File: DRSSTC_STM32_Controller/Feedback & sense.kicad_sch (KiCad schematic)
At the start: 24 parts, among them J8 Screw_Terminal_01x02, J9 Screw_Terminal_01x02

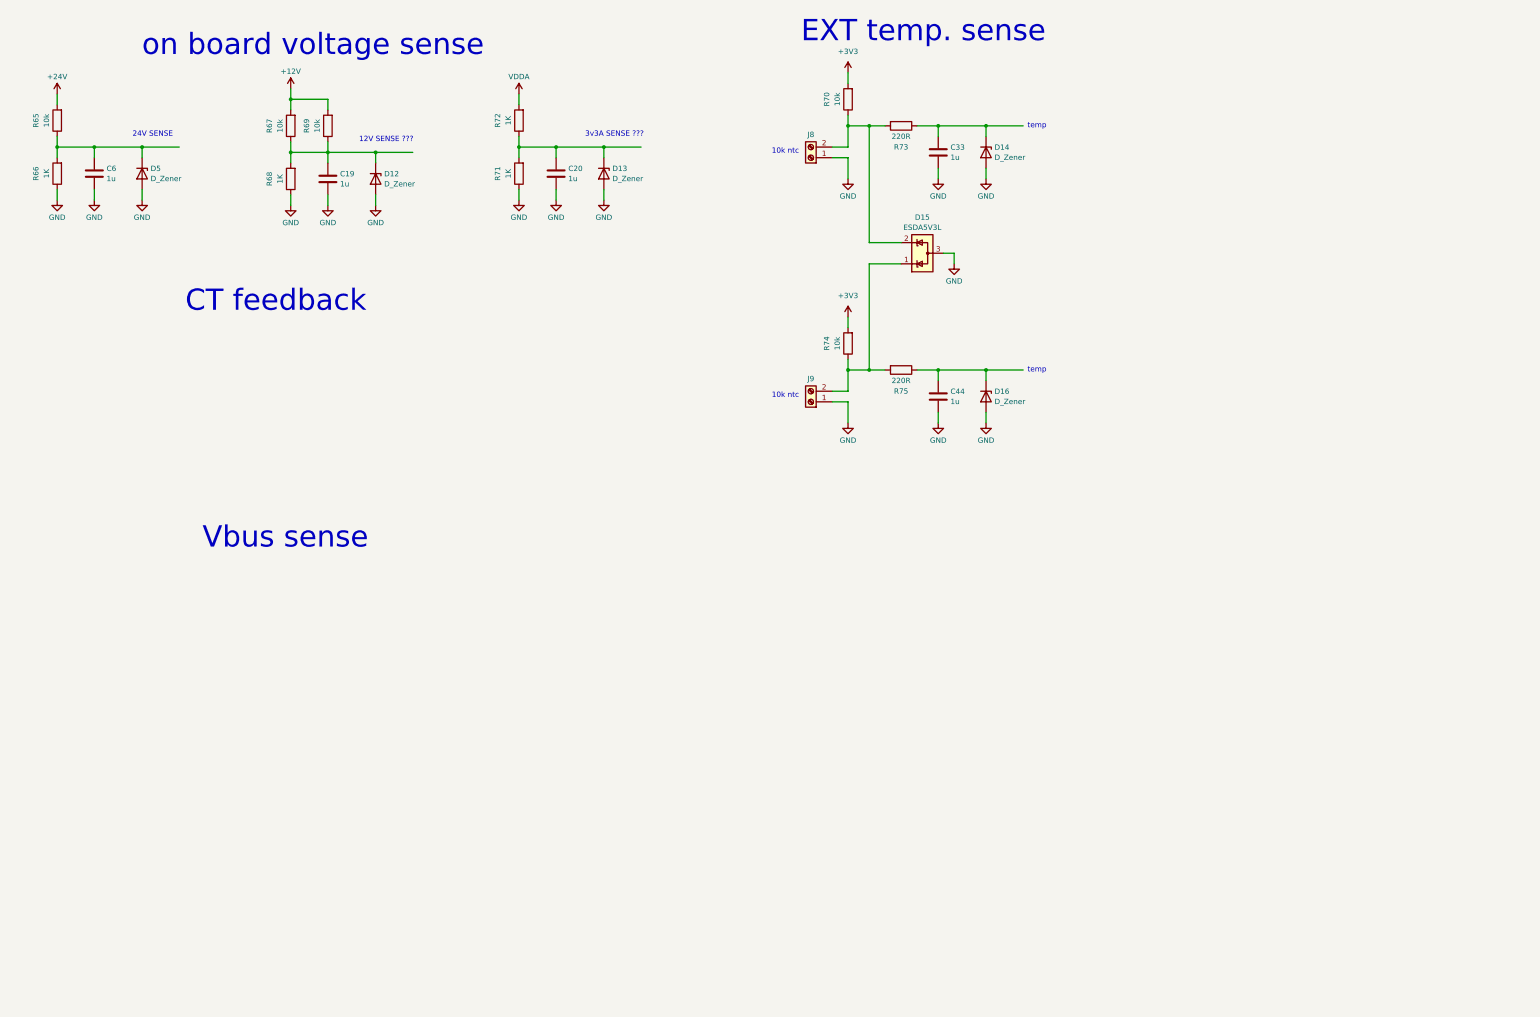
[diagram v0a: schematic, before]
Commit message: update the feedback stage simulation & controller schematic
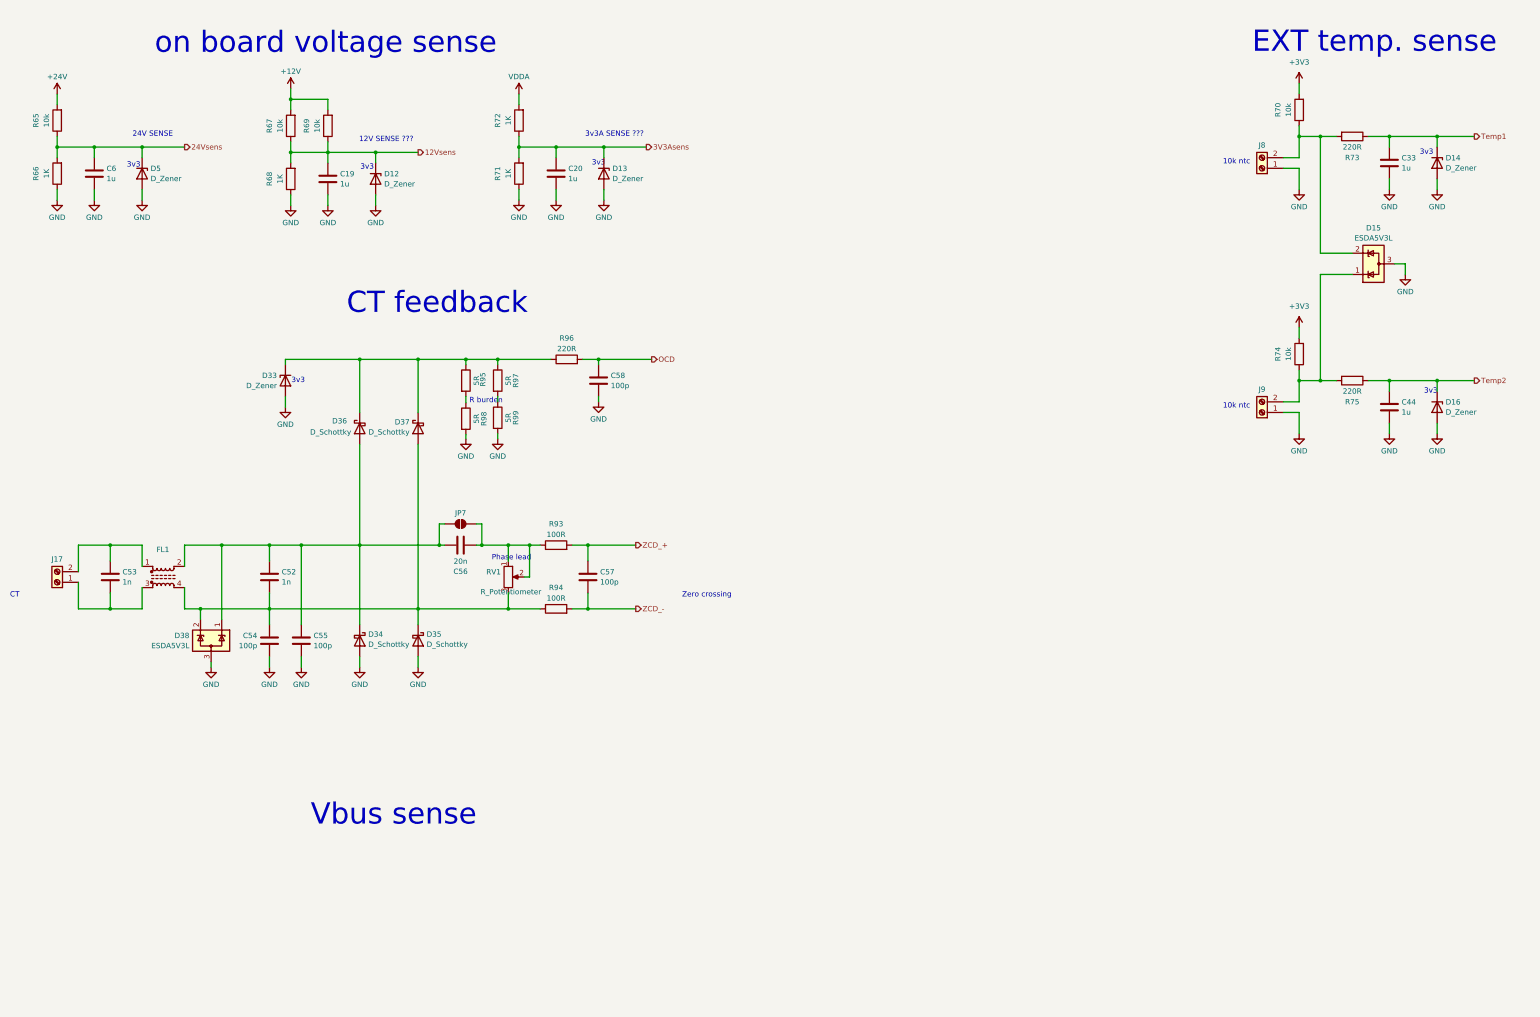
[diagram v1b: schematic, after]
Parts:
- added C52, C53: 1n, symbol Device:C
- added C54, C55, C57, C58: 100p, symbol Device:C
- added C56: 20n, symbol Device:C
- added D33: D_Zener, symbol Device:D_Zener
- added D34, D35, D36, D37: D_Schottky, symbol Device:D_Schottky
- added D38: ESDA5V3L, Package_TO_SOT_SMD:SOT-23-3, symbol Power_Protection:ESDA5V3L
- added FL1: Choke_CommonMode_FerriteCore_1234, symbol Filter:Choke_CommonMode_FerriteCore_1234
- added J17: Screw_Terminal_01x02, TerminalBlock_Altech:Altech_AK100_1x02_P5.00mm, symbol Connector:Screw_Terminal_01x02
- added JP7: SolderJumper_2_Open, Jumper:SolderJumper-2_P1.3mm_Open_RoundedPad1.0x1.5mm, symbol Jumper:SolderJumper_2_Open
- added R93, R94: 100R, Resistor_SMD:R_0805_2012Metric, symbol Device:R
- added R95, R97, R98, R99: 5R, Resistor_SMD:R_0805_2012Metric, symbol Device:R
- added R96: 220R, Resistor_SMD:R_0805_2012Metric, symbol Device:R
- added RV1: R_Potentiometer, symbol Device:R_Potentiometer
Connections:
- net GND: now also C54.2, C55.2, C58.2, D33.2 (A), D34.2 (A), D35.2 (A), D38.3 (A), R98.2, R99.2
- net Temp2: now reaches C44.1, D16.1 (K), R75.1
- net 12Vsens: now reaches C19.1, D12.1 (K), R67.1, R68.2, R69.1
- net 3V3Asens: now reaches C20.1, D13.1 (K), R71.2, R72.1
- net Temp1: now reaches C33.1, D14.1 (K), R73.1
- net 24Vsens: now reaches C6.1, D5.1 (K), R65.1, R66.2
- new net: C53.1, FL1.1, J17.2 (Pin_2)
- new net: C52.1, C55.1, C56.1, D34.1 (K), D36.2 (A), D38.1 (K), FL1.2, JP7.2 (B)
- new net: C53.2, FL1.3, J17.1 (Pin_1)
- new net: C52.2, C54.1, D35.1 (K), D37.2 (A), D38.2 (K), FL1.4, R94.1, RV1.3
- new net: C56.2, JP7.1 (A), R93.1, RV1.1, RV1.2
- new net: D33.1 (K), D36.1 (K), D37.1 (K), R95.1, R96.1, R97.1
- new net: R97.2, R99.1
- new net: R95.2, R98.1
- new net OCD: C58.1, R96.2
- new net ZCD_+: C57.1, R93.2
- new net ZCD_-: C57.2, R94.2
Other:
- note added: "3v3"
- note added: "CT"
- note added: "Phase lead"
- note added: "R burden"
- note added: "Zero crossing"
- note removed: "temp"
- moved on the sheet: C33, C44, D14, D15, D16, J8, J9, R70, R73, R74, R75

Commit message: update conroller schematics
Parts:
- removed J17: Screw_Terminal_01x02, TerminalBlock_Altech:Altech_AK100_1x02_P5.00mm, symbol Connector:Screw_Terminal_01x02
- added C34, C60, C61: 1u, symbol Device:C
- added C62, C65, C81: 100n, symbol Device:C
- added D30, D40, D41, D45, D46: D_Zener, symbol Device:D_Zener
- added D39: ESDA5V3L, Package_TO_SOT_SMD:SOT-23-3, symbol Power_Protection:ESDA5V3L
- added J22, J23: Screw_Terminal_01x02, TerminalBlock_Altech:Altech_AK100_1x02_P5.00mm, symbol Connector:Screw_Terminal_01x02
- added R111, R112, R148, R149: 10k, Resistor_SMD:R_0805_2012Metric, symbol Device:R
- added R113, R114: 220R, Resistor_SMD:R_0805_2012Metric, symbol Device:R
- added R116, R117, R140, R141, R142, R143, R144, R145, R146, R147: 100k, Resistor_SMD:R_1206_3216Metric, symbol Device:R
- added R150, R151: 1K, Resistor_SMD:R_0805_2012Metric, symbol Device:R
- C52: value 1n -> 100p
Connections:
- net +3V3: now also R111.2, R112.2, R150.2
- net GND: now also C34.2, C60.2, C61.2, C62.2, D30.2 (A), D39.3 (A), D40.2 (A), D41.2 (A), D45.2 (A), D46.2 (A), J22.1 (Pin_1), J23.1 (Pin_1), R148.1, R151.1
- net CT+: now reaches C53.1, FL1.1
- net CT-: now reaches C53.2, FL1.3
- new net: R143.2, R144.1
- new net: R144.2, R145.1
- new net: D39.2 (K), J22.2 (Pin_2), R111.1, R113.2
- new net: R146.2, R147.1
- new net: R116.2, R117.1
- new net: R117.2, R140.1
- new net: R145.2, R146.1
- new net: D39.1 (K), J23.2 (Pin_2), R112.1, R114.2
- new net: R141.2, R142.1
- new net: R140.2, R141.1
- new net 3V3sens: C34.1, D30.1 (K), R150.1, R151.2
- new net OPAMP+: C62.1, C81.2, D45.1 (K), R142.2, R148.2
- new net OPAMP-: C65.1, C81.1, D46.1 (K), R147.2, R149.1
- new net OPAMP_out: C65.2, R149.2
- new net Temp3: C60.1, D40.1 (K), R113.1
- new net Temp4: C61.1, D41.1 (K), R114.1
- new net Vbus+: R116.1
- new net Vbus-: R143.1
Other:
- note added: "2.5v"
- note added: "?"
- note added: "additional R on input"
- note added: "analog Phase lead"
- note removed: "12V SENSE ???"
- note removed: "24V SENSE"
- note removed: "3v3A SENSE ???"
- note removed: "CT"
- note removed: "Phase lead"
- moved on the sheet: C19, C20, C33, C44, C52, C53, C54, C55, C56, C57, C58, C6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

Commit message: assign footprints
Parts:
- removed J22, J23, J8, J9: Screw_Terminal_01x02, TerminalBlock_Altech:Altech_AK100_1x02_P5.00mm, symbol Connector:Screw_Terminal_01x02
- removed R116, R117, R140, R141, R143, R144, R145, R146: 100k, Resistor_SMD:R_1206_3216Metric, symbol Device:R
- C19, C20, C33, C34, C44, C52, C53, C54, C55, C56, C57, C58, C60, C61, C62, C65, C81: footprint (none) -> Capacitor_SMD:C_0603_1608Metric
- C6: footprint (none) -> Capacitor_SMD:C_0201_0603Metric
- D12, D13, D14, D16, D30, D33, D40, D41, D45, D46, D5: footprint (none) -> Diode_SMD:D_SOD-323F
- D34, D35, D36, D37: footprint (none) -> Diode_SMD:D_SOD-128
- FL1: footprint (none) -> Button_Switch_SMD:SW_MEC_5GSH9
- R111, R112, R113, R114, R148, R149, R150, R151, R65, R66, R67, R68, R69, R70, R71, R72, R73, R74, R75, R93, R94, R96: footprint Resistor_SMD:R_0805_2012Metric -> Resistor_SMD:R_0603_1608Metric
- R142, R147: value 100k -> 10K; footprint Resistor_SMD:R_1206_3216Metric -> Resistor_SMD:R_0603_1608Metric
- R95, R97, R98, R99: footprint Resistor_SMD:R_0805_2012Metric -> Resistor_SMD:R_1206_3216Metric
- RV1: footprint (none) -> Potentiometer_THT:Potentiometer_ACP_CA6-H2,5_Horizontal
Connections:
- net Vbus+: now also R142.1
- net Vbus-: now also R147.1
- net NTC3: now reaches D39.2 (K), R111.1, R113.2
- net NTC2: now reaches D15.1 (K), R74.1, R75.2
- net NTC1: now reaches D15.2 (K), R70.1, R73.2
- net NTC4: now reaches D39.1 (K), R112.1, R114.2
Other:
- note added: "DDZ3V0ASF-7"

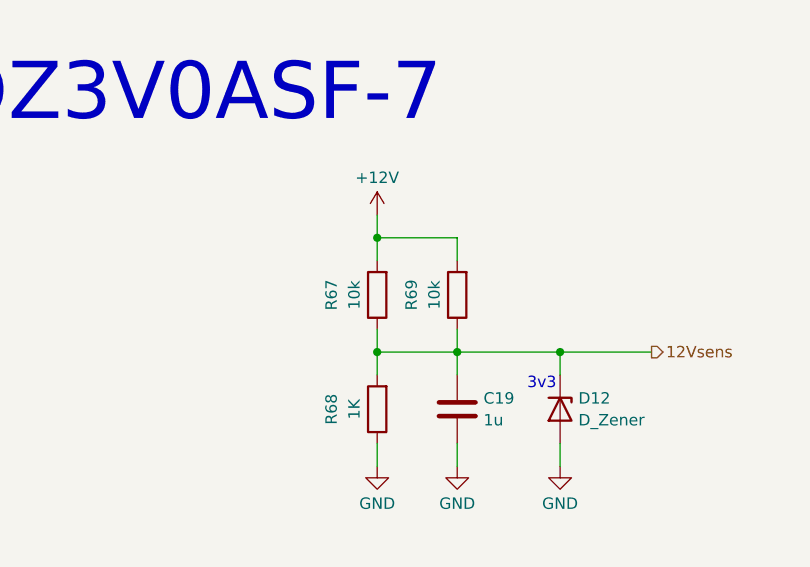
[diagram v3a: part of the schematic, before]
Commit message: start cintrollenr routing
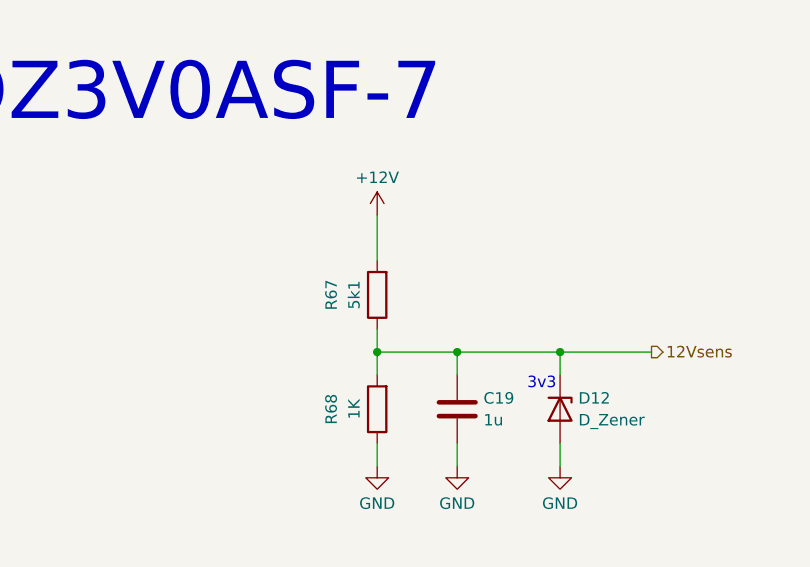
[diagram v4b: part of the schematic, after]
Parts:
- removed R69: 10k, Resistor_SMD:R_0603_1608Metric, symbol Device:R
- C6: footprint Capacitor_SMD:C_0201_0603Metric -> Capacitor_SMD:C_0603_1608Metric
- R67: value 10k -> 5k1
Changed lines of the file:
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@@
 	)
 	(junction
-		(at 236.22 161.29)
-		(diameter 0)
-		(color 0 0 0 0)
-	)
-	(junction
 		(at 345.44 214.63)
 		(diameter 0)
@@
 	(wire
 		(pts
-			(xy 245.11 161.29) (xy 236.22 161.29)
-		)
-		(stroke
-			(width 0)
-			(type default)
-		)
-	)
-	(wire
-		(pts
 			(xy 140.97 73.66) (xy 140.97 74.93)
 		)
@@
 	(wire
 		(pts
-			(xy 236.22 158.75) (xy 236.22 161.29)
+			(xy 236.22 158.75) (xy 236.22 163.83)
 		)
 		(stroke
@@
 	(wire
 		(pts
-			(xy 245.11 163.83) (xy 245.11 161.29)
-		)
-		(stroke
-			(width 0)
-			(type default)
-		)
-	)
-	(wire
-		(pts
 			(xy 328.93 48.26) (xy 328.93 76.2)
 		)
@@
 	(wire
 		(pts
-			(xy 245.11 171.45) (xy 245.11 173.99)
-		)
-		(stroke
-			(width 0)
-			(type default)
-		)
-	)
-	(wire
-		(pts
 			(xy 158.75 115.57) (xy 162.56 115.57)
 		)
@@
 	(wire
 		(pts
-			(xy 236.22 163.83) (xy 236.22 161.29)
-		)
-		(stroke
-			(width 0)
-			(type default)
-		)
-	)
-	(wire
-		(pts
 			(xy 328.93 106.68) (xy 332.74 106.68)
 		)
@@
 			)
 		)
-		(property "Value" "10k"
+		(property "Value" "5k1"
 			(at 233.68 167.64 90)
 			(show_name no)
@@
 	)
 	(symbol
-		(lib_id "Device:R")
-		(at 245.11 167.64 180)
-		(unit 1)
-		(body_style 1)
-		(exclude_from_sim no)
-		(in_bom yes)
-		(on_board yes)
-		(in_pos_files yes)
-		(dnp no)
-		(property "Reference" "R69"
-			(at 240.03 167.64 90)
-			(show_name no)
-			(do_not_autoplace no)
-			(effects
-				(font
-					(size 1.27 1.27)
-				)
-			)
-		)
-		(property "Value" "10k"
-			(at 242.57 167.64 90)
-			(show_name no)
-			(do_not_autoplace no)
-			(effects
-				(font
-					(size 1.27 1.27)
-				)
-			)
-		)
-		(property "Footprint" "Resistor_SMD:R_0603_1608Metric"
-			(at 246.888 167.64 90)
-			(hide yes)
-			(show_name no)
-			(do_not_autoplace no)
-			(effects
-				(font
-					(size 1.27 1.27)
-				)
-			)
-		)
-		(property "Datasheet" ""
-			(at 245.11 167.64 0)
-			(hide yes)
-			(show_name no)
-			(do_not_autoplace no)
-			(effects
-				(font
-					(size 1.27 1.27)
-				)
-			)
-		)
-		(property "Description" "Resistor"
-			(at 245.11 167.64 0)
-			(hide yes)
-			(show_name no)
-			(do_not_autoplace no)
-			(effects
-				(font
-					(size 1.27 1.27)
-				)
-			)
-		)
-		(pin "1"
-		)
-		(pin "2"
-		)
-		(instances
-			(project "DRSSTC_STM32_Controller"
-				(path "/1b08b5a8-62c7-4a0a-af72-03cffe829476/f36fd572-7bba-4e39-aaf8-4f152063ad7b"
-					(reference "R69")
-					(unit 1)
-				)
-			)
-		)
-	)
-	(symbol
 		(lib_id "Filter:Choke_CommonMode_FerriteCore_1234")
 		(at 60.96 107.95 0)
@@
 			)
 		)
-		(property "Footprint" "Capacitor_SMD:C_0201_0603Metric"
+		(property "Footprint" "Capacitor_SMD:C_0603_1608Metric"
 			(at 246.0752 246.38 0)
 			(hide yes)
